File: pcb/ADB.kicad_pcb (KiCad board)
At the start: 2 copper layers, 77.2 x 50.8 mm, 54 parts, among them J1 Conn_01x10_Socket, J10 Conn_02x02_Counter_Clockwise, J11 Conn_02x02_Counter_Clockwise, J12 Conn_02x02_Counter_Clockwise, J13 Conn_02x02_Counter_Clockwise, J14 Conn_01x02_Socket, J15 Conn_01x04_Socket, J16 Conn_01x02_Socket, J17 Conn_01x02_Socket, J18 Conn_01x02_Socket, J19 Conn_01x03_Socket, J2 Conn_01x03_Pin, J20 Conn_01x03_Socket, J21 Conn_01x02_Socket, J22 Conn_01x02_Socket, J23 Conn_01x04_Socket, J24 Conn_01x02_Socket, J25 Conn_01x02_Socket, J26 Conn_01x02_Socket, J27 Conn_01x02_Socket, J28 Conn_01x02_Socket, J29 Conn_01x02_Socket, J3 Conn_01x08_Pin, J30 Conn_01x04_Socket, J31 Conn_01x02_Socket, J32 Conn_01x02_Socket, J33 Conn_01x02_Socket, J34 Conn_01x03_Socket, J35 Conn_01x03_Socket, J36 Conn_01x02_Socket, J37 Conn_01x02_Socket, J38 Conn_01x04_Socket, J39 Conn_01x02_Socket, J4 Conn_01x02_Pin, J40 Conn_01x02_Socket, J41 Conn_01x02_Socket, J42 Conn_01x02_Socket, J43 Conn_01x02_Socket, J5 Conn_01x10_Socket, J6 Conn_02x02_Counter_Clockwise, J7 Conn_02x02_Counter_Clockwise, J8 Conn_02x02_Counter_Clockwise, J9 Conn_02x02_Counter_Clockwise, U1 LM358

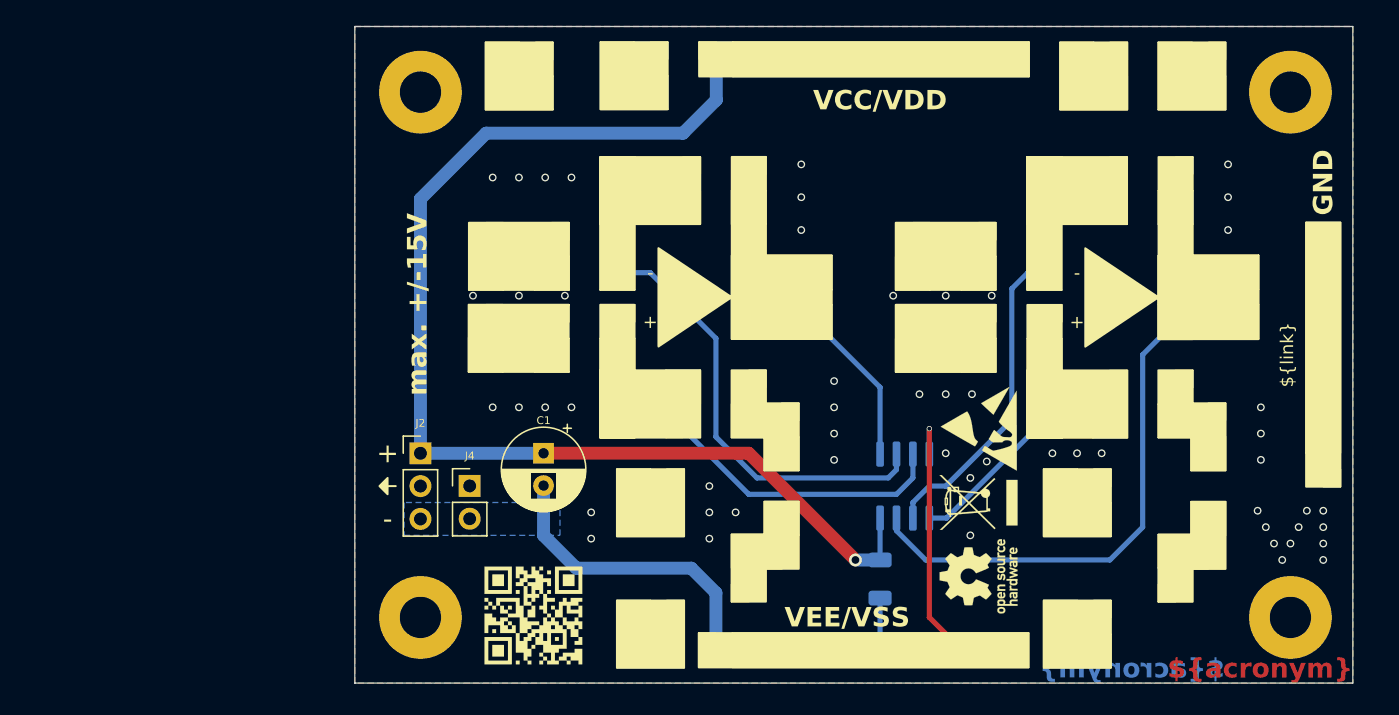
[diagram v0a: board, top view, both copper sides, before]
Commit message: Adapt edge cuts and dimensioning
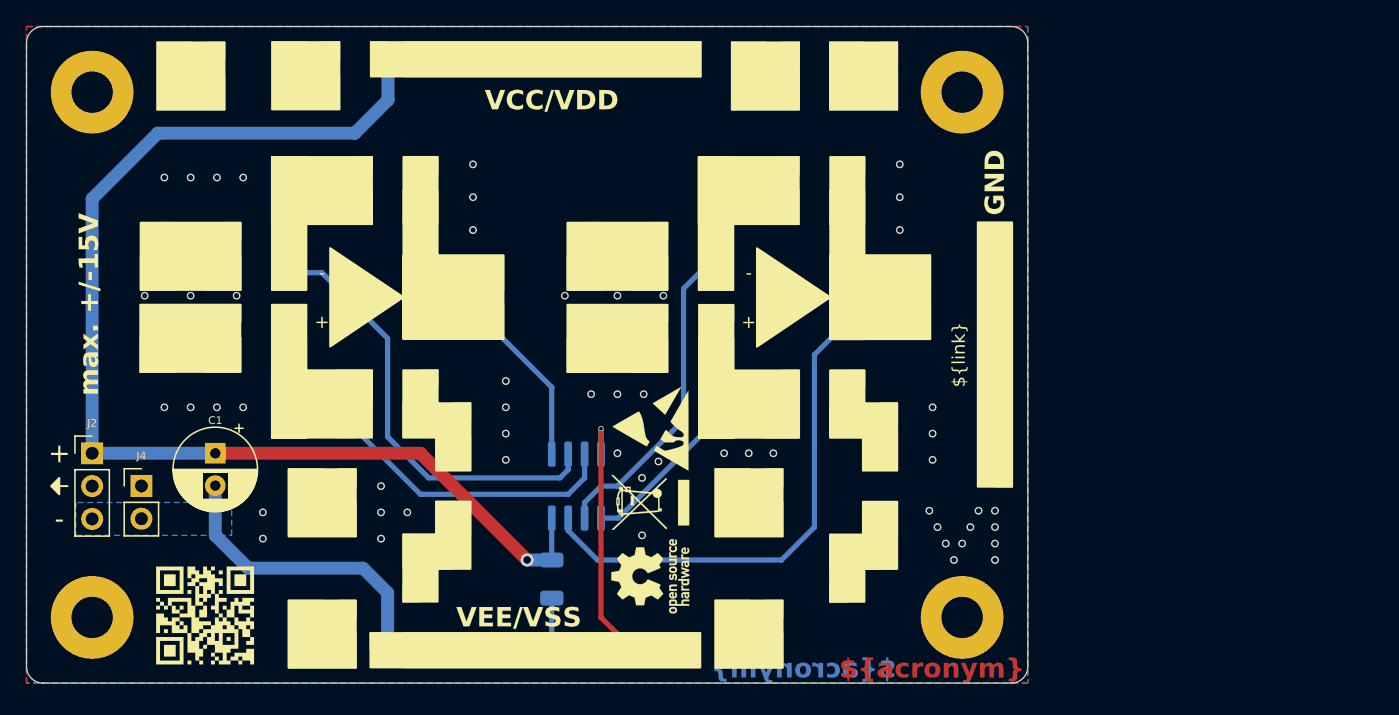
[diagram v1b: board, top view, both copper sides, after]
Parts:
- moved H1 25.4 mm to (124.5, 81.3)
- moved H2 25.4 mm to (124.5, 121.9)
- moved J2 25.4 mm to (124.5, 109.2)
- moved FID1 25.4 mm to (167.6, 107.3)
- moved FID2 25.4 mm to (167.6, 113.0)
- moved FID3 25.4 mm to (167.6, 118.7)
- moved FID4 25.4 mm to (133.3, 121.9)
- moved J1 25.4 mm to (147.3, 78.7)
- moved J10 25.4 mm to (143.5, 121.9)
- moved J11 25.4 mm to (143.5, 111.8)
- moved J14 25.4 mm to (144.8, 87.6)
- moved J15 25.4 mm to (139.7, 87.6)
- moved J17 25.4 mm to (129.5, 92.7)
- moved J18 25.4 mm to (134.6, 92.7)
- moved J19 25.4 mm to (149.9, 99.0)
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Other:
- board size 77.2 x 50.8 mm -> 77.5 x 50.8 mm

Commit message: Add reverse polarity protection
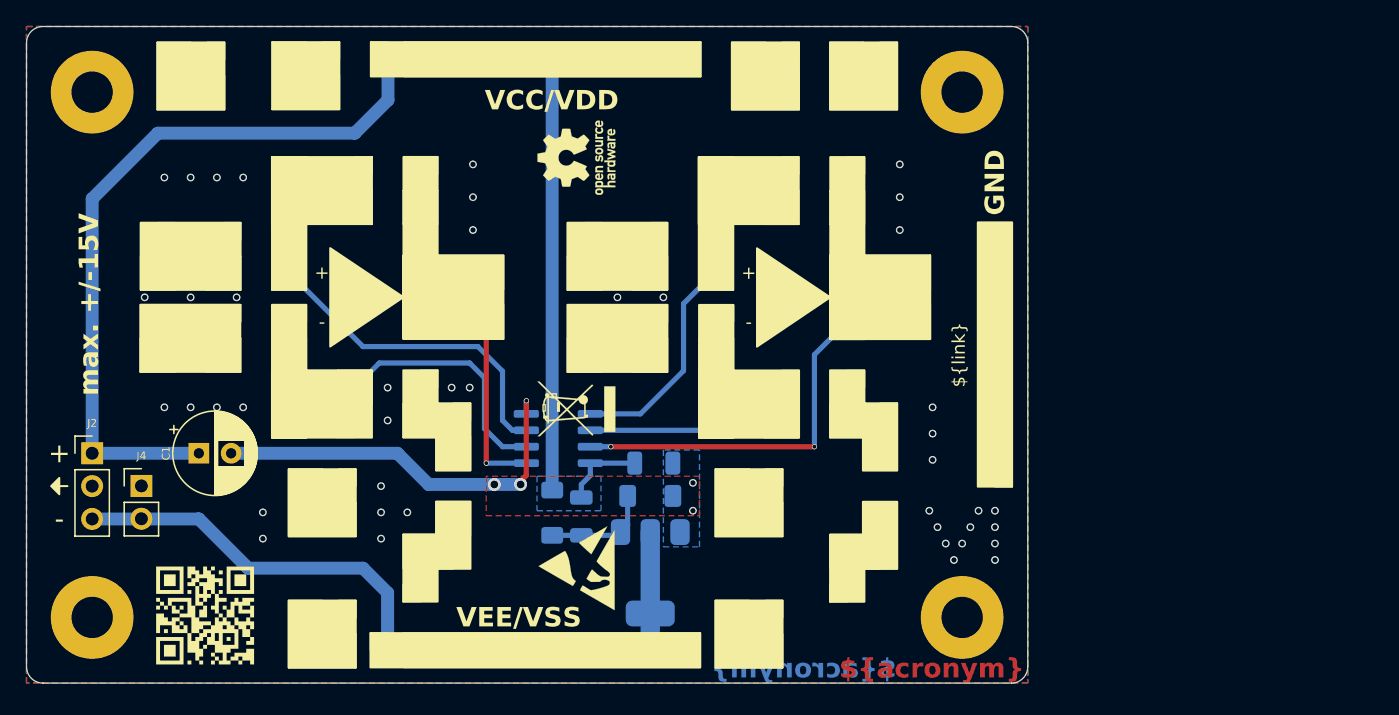
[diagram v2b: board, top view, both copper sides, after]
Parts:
- added D1: BAT43, Diode_SMD:D_MiniMELF, B.Cu at (160.1, 113.8)
- added D2: BZ5V1, Diode_SMD:D_MiniMELF, B.Cu at (167.6, 112.5)
- added Q1: BUK7880-55A, Package_TO_SOT_SMD:SOT-223-3_TabPin2, B.Cu at (167.6, 118.5)
- added R1: 1k, Resistor_SMD:R_1206_3216Metric, B.Cu at (162.3, 114.1)
- moved FID3 32.9 mm to (161.9, 86.4)
- moved FID1 12.2 mm to (161.9, 118.1)
- moved C2 11.9 mm to (167.9, 110.0), turned to 0 degrees
- moved FID2 9.22 mm to (161.9, 105.8)
- moved U1 3.94 mm to (160.5, 108.1), turned to 0 degrees
- moved C1 1.27 mm to (132.7, 109.2), turned to 0 degrees
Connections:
- C1 pad 2: VEE -> Net-(D2-A)
- C2 pad 2: VEE -> Net-(D2-A)
- U1 pad 2: Net-(J14-Pin_1) -> Net-(J23-Pin_1)
- U1 pad 3: Net-(J23-Pin_1) -> Net-(J14-Pin_1)
- U1 pad 4: VEE -> Net-(D2-A)
- U1 pad 5: Net-(J38-Pin_1) -> Net-(J29-Pin_1)
- U1 pad 6: Net-(J29-Pin_1) -> Net-(J38-Pin_1)
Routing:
- net Net-(D2-A): track 0.00 -> 30.9 mm, vias 0 -> 5
- net Net-(J31-Pin_1): track 39.0 -> 28.1 mm, vias 0 -> 2
- net Net-(D1-A): track 0.00 -> 8.93 mm
- net Net-(J14-Pin_1): track 34.1 -> 25.6 mm
- net VEE: track 47.1 -> 38.8 mm, vias 1 -> 0
- net Net-(J29-Pin_1): track 24.7 -> 17.3 mm
- net VCC: track 91.1 -> 96.9 mm, vias 1 -> 0
- net Net-(J23-Pin_1): track 22.9 -> 19.0 mm
- net Net-(J38-Pin_1): track 12.0 -> 10.1 mm
- net Net-(J16-Pin_1): track 12.3 -> 14.0 mm, vias 0 -> 1
- net GND: vias 54 -> 43
- added copper zone on B.Cu, net Net-(D2-A)
- added copper zone on F.Cu, net Net-(D2-A)
